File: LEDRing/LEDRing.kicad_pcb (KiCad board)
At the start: 2 copper layers, 26 x 20.7 mm, 7 parts, among them J1 V+, J2 V-

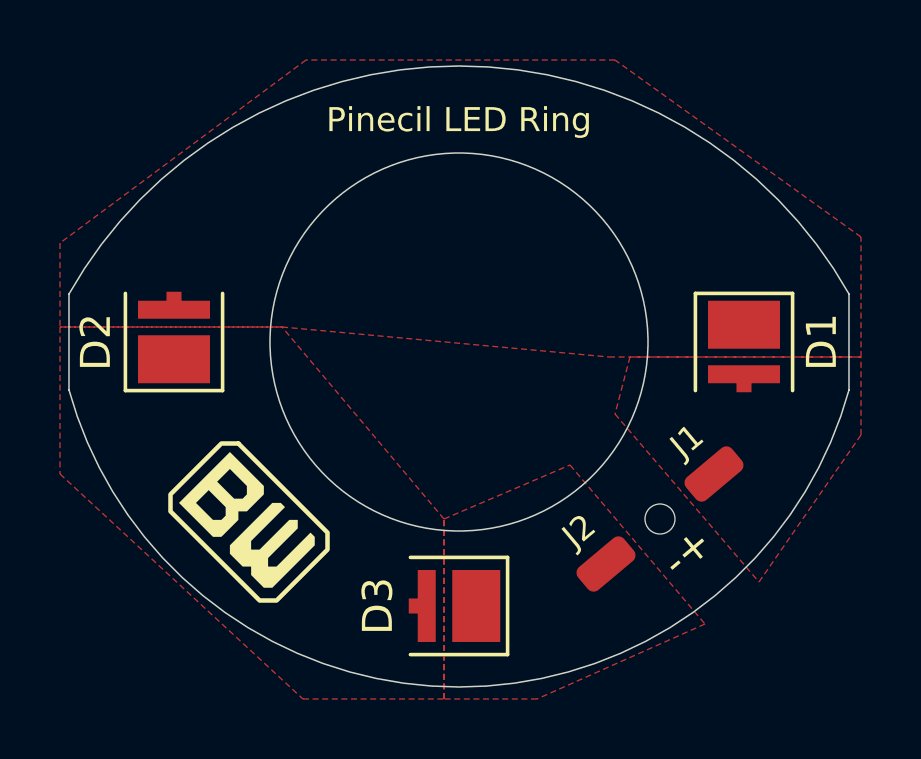
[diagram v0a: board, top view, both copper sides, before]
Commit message: Ring hole size increased
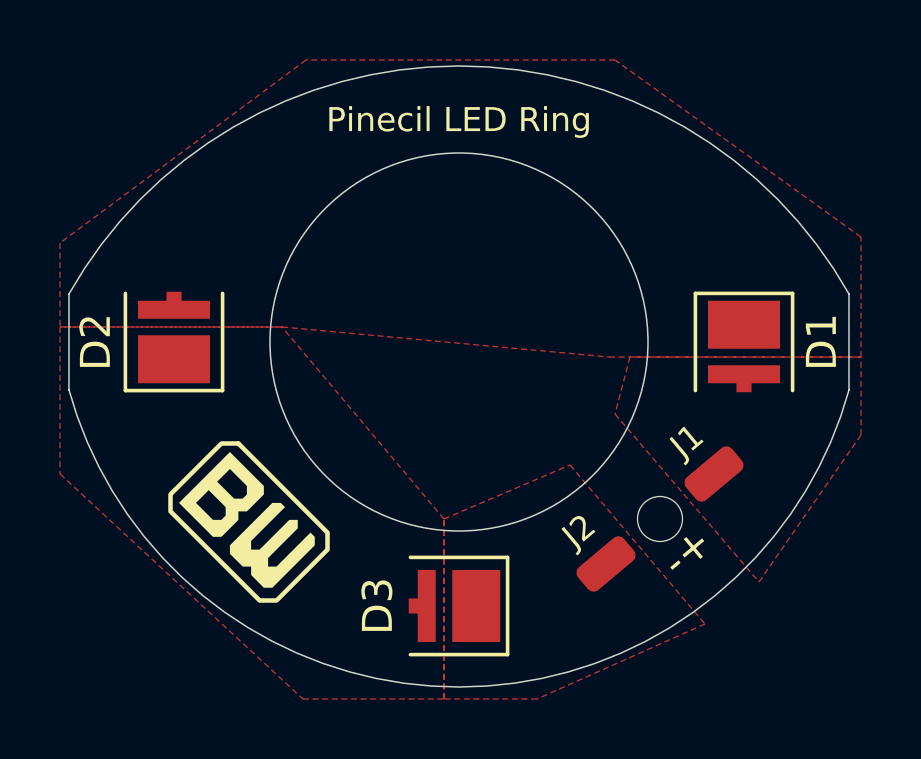
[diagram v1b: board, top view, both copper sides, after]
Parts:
- D1, D2, D3: value LED 0.2W -> MP-3030
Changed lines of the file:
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@@
 			)
 		)
-		(property "Value" "LED 0.2W"
+		(property "Value" "MP-3030"
 			(at 0 2.7 90)
 			(layer "F.Fab")
@@
 		(pad "" np_thru_hole circle
 			(at 0 0)
-			(size 1 1)
-			(drill 1)
+			(size 1.5 1)
+			(drill 1.5)
 			(layers "F&B.Cu" "*.Mask")
 		)
@@
 			)
 		)
-		(property "Value" "LED 0.2W"
+		(property "Value" "MP-3030"
 			(at 0 2.7 -90)
 			(layer "F.Fab")
@@
 			)
 		)
-		(property "Value" "LED 0.2W"
+		(property "Value" "MP-3030"
 			(at 0 2.7 180)
 			(layer "F.Fab")
@@
 		(end 156.55 100)
 		(stroke
-			(width 0)
+			(width 0.1)
 			(type default)
 		)
@@
 				(xy 155.246126 104.326449) (xy 155.56192 103.912167) (xy 155.845073 103.474927) (xy 156.093926 103.017295)
 				(xy 156.307017 102.541956) (xy 156.483095 102.0517) (xy 156.621129 101.549404) (xy 156.720307 101.038015)
-				(xy 156.780047 100.520535) (xy 156.8 100)
-			)
-		)
+				(xy 156.780047 100.520535)
+			)
+		)
